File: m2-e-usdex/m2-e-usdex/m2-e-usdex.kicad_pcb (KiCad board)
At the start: 6 copper layers, 22 x 80 mm, 10 parts, among them J1 Bus_M.2_Socket_M, J2 Micro_SDex_Card_Det1, U1 AMS1117-1.8

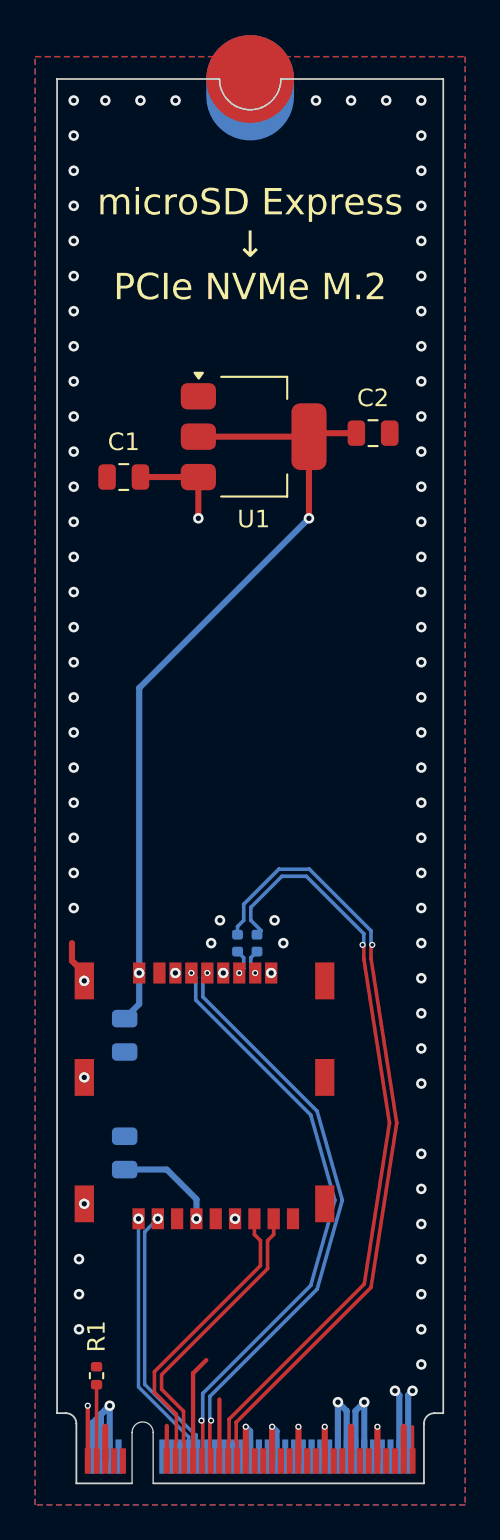
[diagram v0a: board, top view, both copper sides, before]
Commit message: m2-e-usdex: Create fillets
I did this in a separate commit, because this can't be undone and
creating the free angle differential lines was a very long, painful and
manual process.
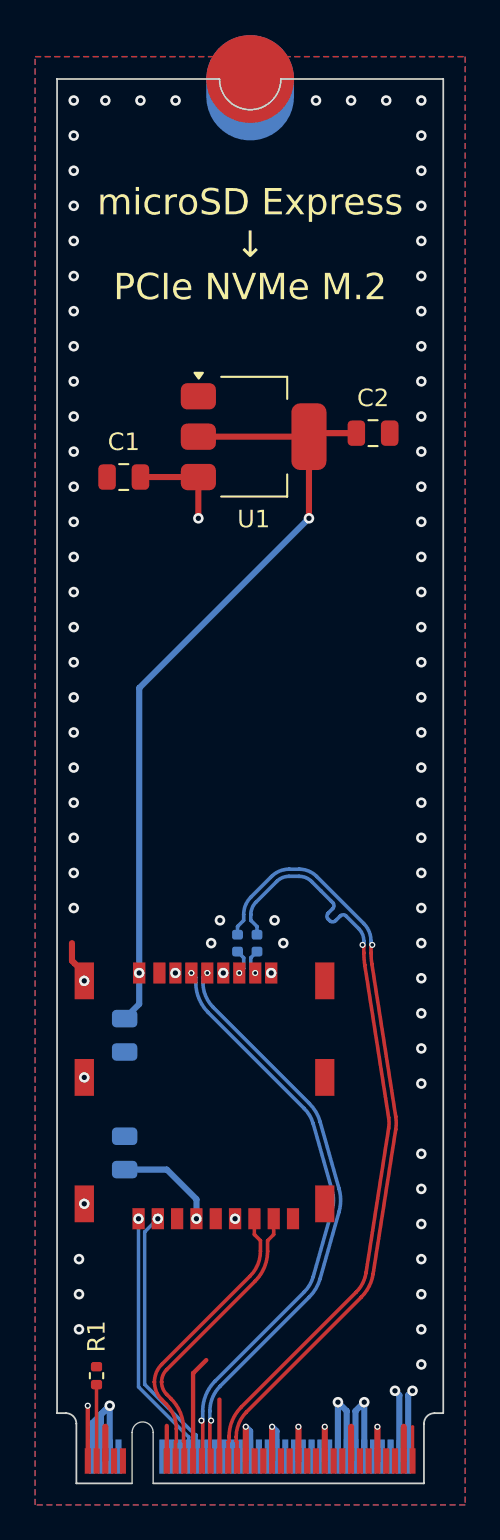
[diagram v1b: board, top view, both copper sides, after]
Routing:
- net PCIe_RX+: track 44.0 -> 44.6 mm

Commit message: m2-e-usdex: add testpoint and fill planes
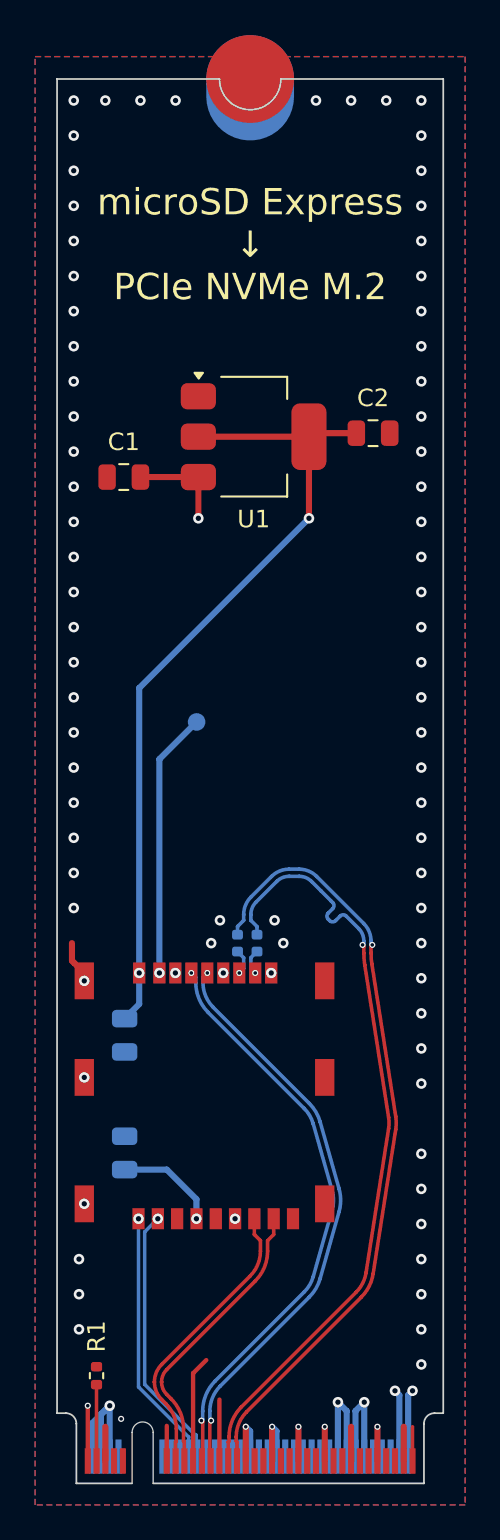
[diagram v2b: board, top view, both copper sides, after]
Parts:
- added TP1: TestPoint, TestPoint:TestPoint_Pad_D1.0mm, B.Cu at (266.2, 93.4)
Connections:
- J2 pad 17: unconnected-(J2-1V2-Pad17) -> Net-(J2-1V2)
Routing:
- net Net-(J2-1V2): track 0.00 -> 15.2 mm, vias 0 -> 1
- net GND: vias 86 -> 87
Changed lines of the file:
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@@
 	(net 41 "unconnected-(J1-~{PLA_S3}{slash}NC-Pad30)")
 	(net 42 "+1V8")
-	(net 43 "unconnected-(J2-1V2-Pad17)")
+	(net 43 "Net-(J2-1V2)")
 	(net 44 "unconnected-(J2-CLK-Pad5)")
 	(net 45 "unconnected-(J2-CMD-Pad3)")
@@
 			(size 0.7 1.2)
 			(layers "F.Cu" "F.Mask" "F.Paste")
-			(net 43 "unconnected-(J2-1V2-Pad17)")
+			(net 43 "Net-(J2-1V2)")
 			(pinfunction "1V2")
-			(pintype "power_in+no_connect")
+			(pintype "power_in")
 			(thermal_bridge_angle 45)
 		)
@@
 		)
 	)
+	(footprint "TestPoint:TestPoint_Pad_D1.0mm"
+		(layer "B.Cu")
+		(at 266.2 93.4 180)
+		(descr "SMD pad as test Point, diameter 1.0mm")
+		(tags "test point SMD pad")
+		(property "Reference" "TP1"
+			(at 0 1.448 0)
+			(layer "B.SilkS")
+			(effects
+				(font
+					(size 1 1)
+					(thickness 0.15)
+				)
+				(justify mirror)
+			)
+		)
+		(property "Value" "TestPoint"
+			(at 0 -1.55 0)
+			(layer "B.Fab")
+			(effects
+				(font
+					(size 1 1)
+					(thickness 0.15)
+				)
+				(justify mirror)
+			)
+		)
+		(property "Datasheet" ""
+			(at 0 0 0)
+			(unlocked yes)
+			(layer "B.Fab")
+			(hide yes)
+			(effects
+				(font
+					(size 1.27 1.27)
+					(thickness 0.15)
+				)
+				(justify mirror)
+			)
+		)
+		(property "Description" "test point"
+			(at 0 0 0)
+			(unlocked yes)
+			(layer "B.Fab")
+			(hide yes)
+			(effects
+				(font
+					(size 1.27 1.27)
+					(thickness 0.15)
+				)
+				(justify mirror)
+			)
+		)
+		(property ki_fp_filters "Pin* Test*")
+		(sheetname "/")
+		(sheetfile "m2-e-usdex.kicad_sch")
+		(attr exclude_from_pos_files)
+		(fp_circle
+			(center 0 0)
+			(end 0 -0.7)
+			(stroke
+				(width 0.12)
+				(type solid)
+			)
+			(fill no)
+			(layer "B.SilkS")
+		)
+		(fp_circle
+			(center 0 0)
+			(end 1 0)
+			(stroke
+				(width 0.05)
+				(type solid)
+			)
+			(fill no)
+			(layer "B.CrtYd")
+		)
+		(fp_text user "${REFERENCE}"
+			(at 0 1.45 0)
+			(layer "B.Fab")
+			(effects
+				(font
+					(size 1 1)
+					(thickness 0.15)
+				)
+				(justify mirror)
+			)
+		)
+		(pad "1" smd circle
+			(at 0 0 180)
+			(size 1 1)
+			(layers "B.Cu" "B.Mask")
+			(net 43 "Net-(J2-1V2)")
+			(pinfunction "1")
+			(pintype "passive")
+		)
+		(embedded_fonts no)
+	)
 	(footprint "Capacitor_SMD:C_0805_2012Metric"
 		(layer "B.Cu")
@@
 	)
 	(via
+		(at 261.9 133.1)
+		(size 0.35)
+		(drill 0.2)
+		(layers "F.Cu" "B.Cu")
+		(free yes)
+		(net 11)
+	)
+	(via
 		(at 279 88)
 		(size 0.6)
@@
 	)
 	(via
+		(at 264.08 107.7)
+		(size 0.6)
+		(drill 0.3)
+		(layers "F.Cu" "B.Cu")
+		(net 43)
+	)
+	(segment
+		(start 266.2 93.4)
+		(end 264.08 95.52)
+		(width 0.35)
+		(layer "B.Cu")
+		(net 43)
+	)
+	(segment
+		(start 264.08 95.52)
+		(end 264.08 107.7)
+		(width 0.35)
+		(layer "B.Cu")
+		(net 43)
+	)
+	(via
 		(at 268.63 107.7)
 		(size 0.35)
@@
 		(min_thickness 0.25)
 		(filled_areas_thickness no)
-		(fill
+		(fill yes
 			(thermal_gap 0.5)
 			(thermal_bridge_width 0.5)
@@
 		(min_thickness 0.25)
 		(filled_areas_thickness no)
-		(fill
+		(fill yes
 			(thermal_gap 0.5)
 			(thermal_bridge_width 0.5)
@@
 		(min_thickness 0.25)
 		(filled_areas_thickness no)
-		(fill
+		(fill yes
 			(thermal_gap 0.5)
 			(thermal_bridge_width 0.5)
@@
 		(min_thickness 0.25)
 		(filled_areas_thickness no)
-		(fill
+		(fill yes
 			(thermal_gap 0.5)
 			(thermal_bridge_width 0.5)
@@
 		(min_thickness 0.25)
 		(filled_areas_thickness no)
-		(fill
+		(fill yes
 			(thermal_gap 0.5)
 			(thermal_bridge_width 0.5)
@@
 		(min_thickness 0.25)
 		(filled_areas_thickness no)
-		(fill
+		(fill yes
 			(thermal_gap 0.5)
 			(thermal_bridge_width 0.5)
